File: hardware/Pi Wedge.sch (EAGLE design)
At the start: 9 parts

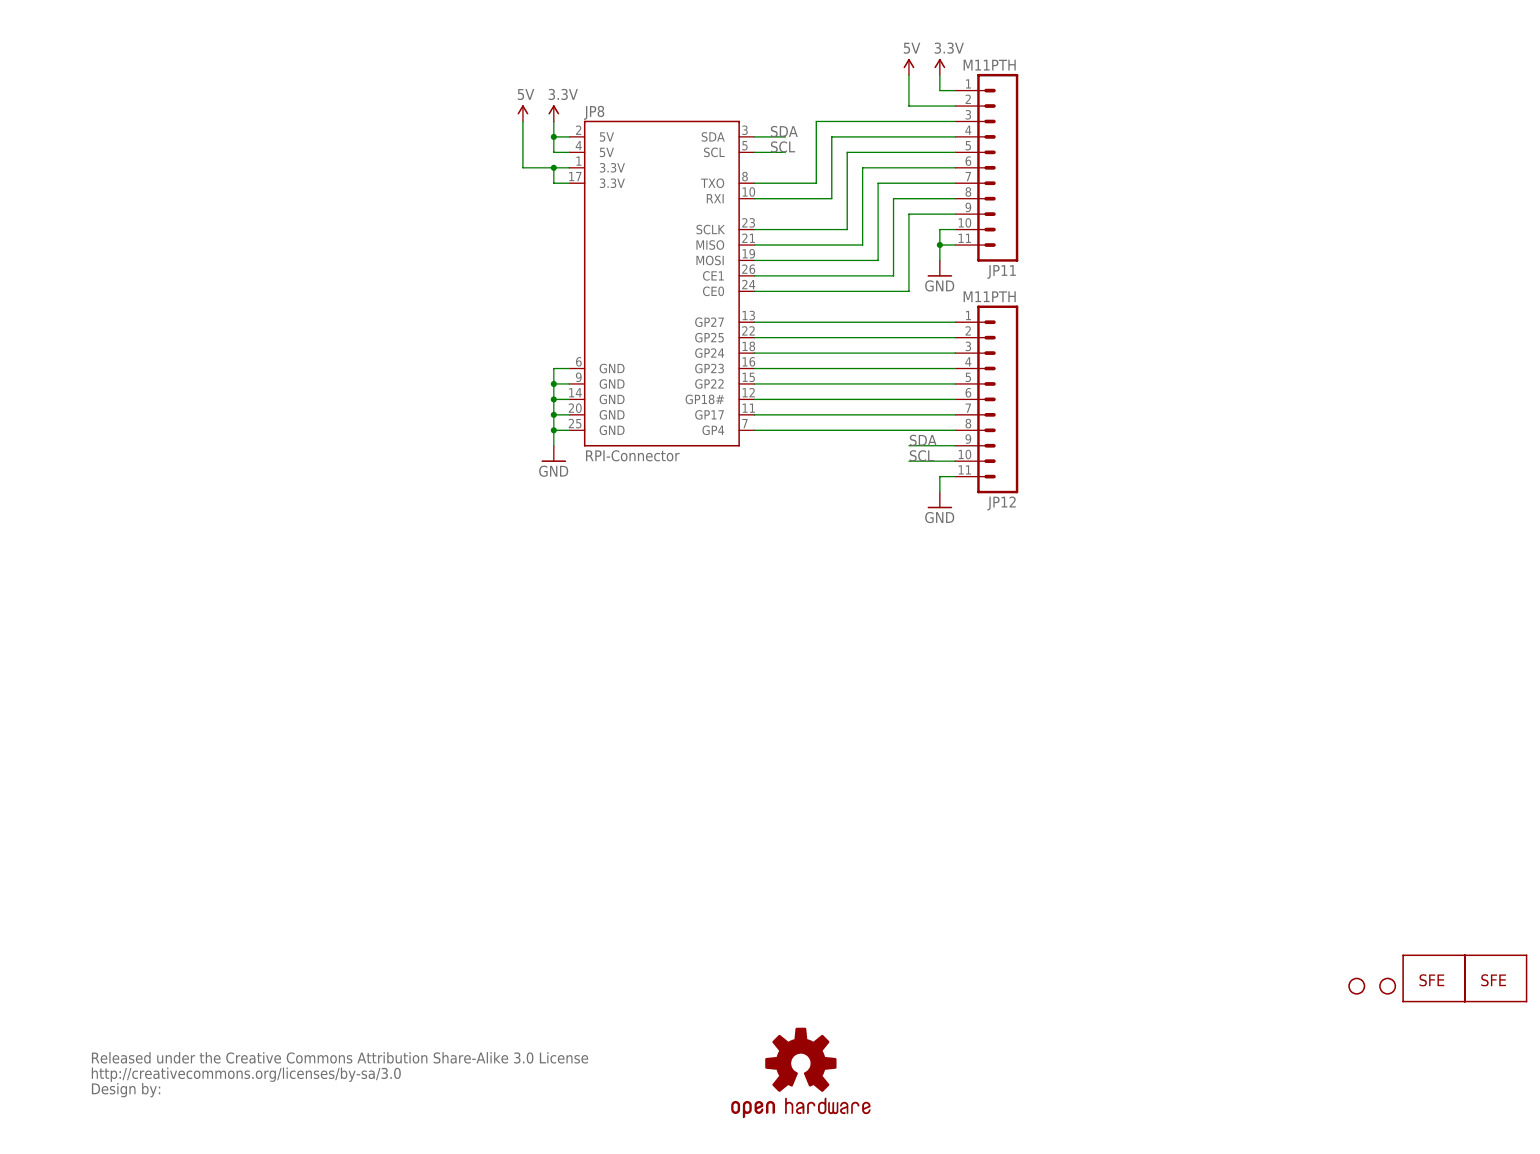
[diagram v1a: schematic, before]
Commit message: Adjusting everything.
Reoriented connectors, added 6-pin FTDI header and extra access to power
and ground.
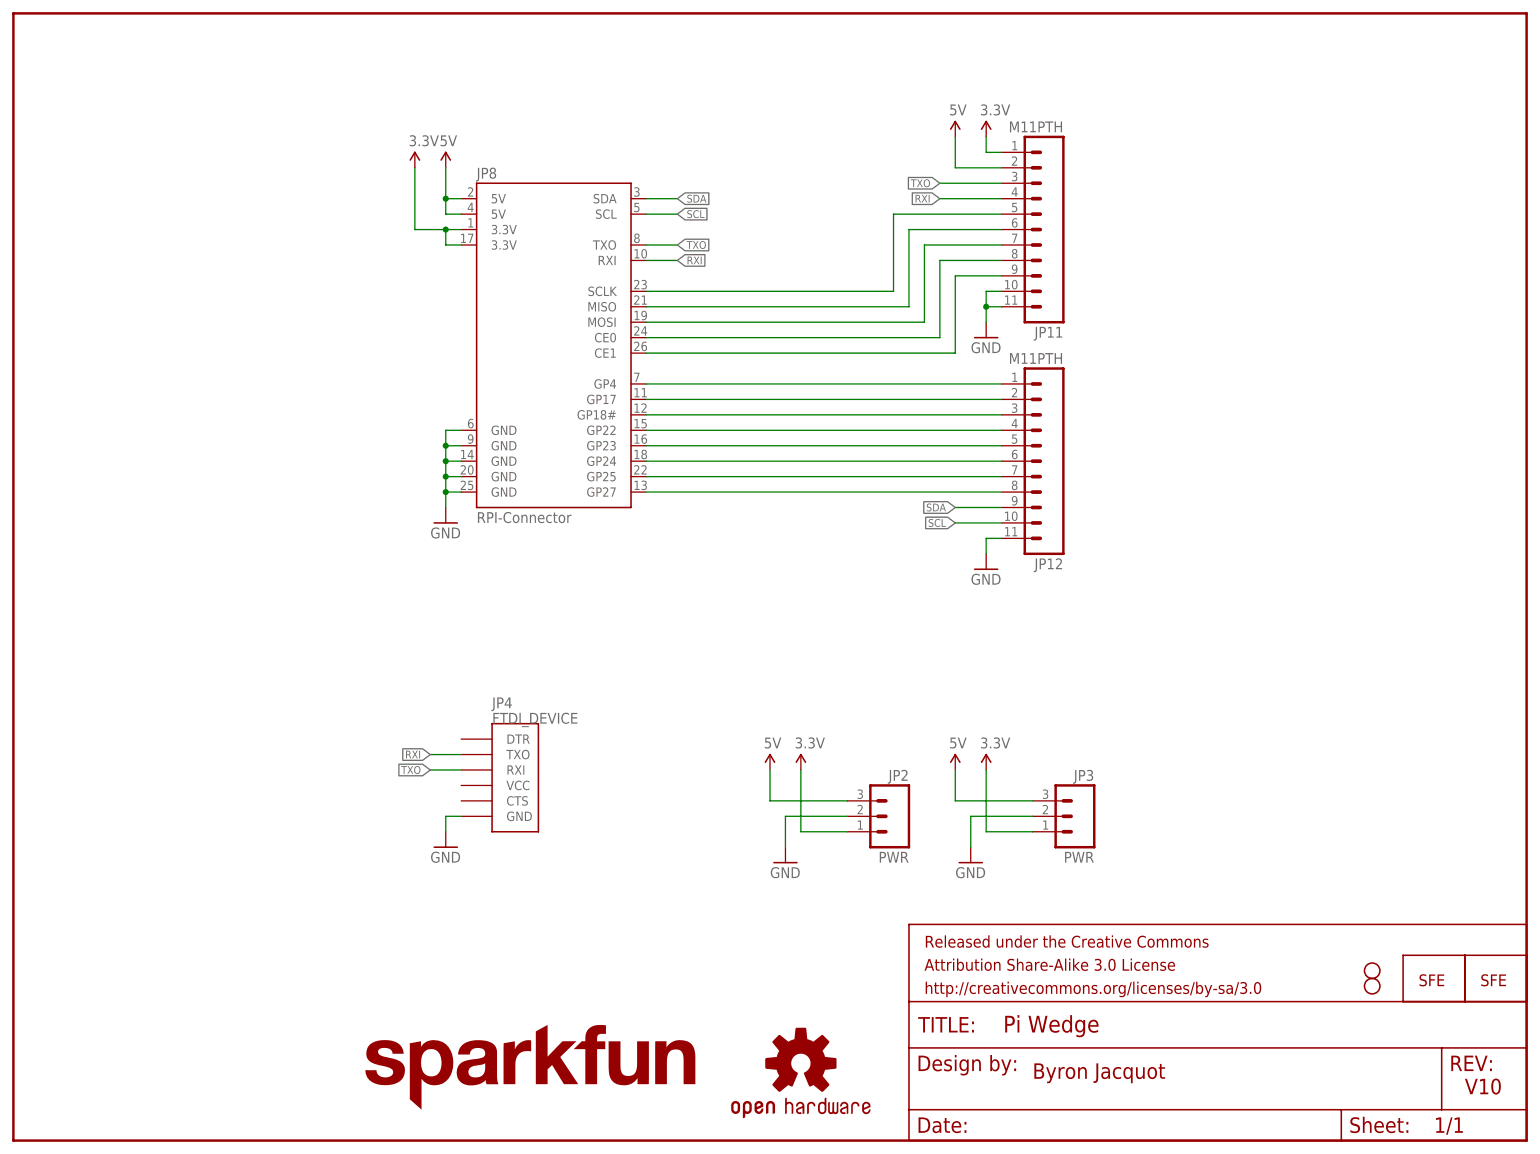
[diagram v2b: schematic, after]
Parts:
- removed U$2: CREATIVE_COMMONS, SparkFun:CREATIVE_COMMONS
- added FRAME2: FRAME-LETTER, SparkFun-Aesthetics:FRAME-LETTER
- added JP4: FTDI_DEVICE, SparkFun-Connectors:FTDI_DEVICE
- added LOGO1: SFE_LOGO_NAME.2_INCH, SparkFun-Aesthetics:SFE_LOGO_NAME.2_INCH
- added STANDOFF1, STANDOFF2: STAND-OFF, SparkFun-Electromechanical:STAND-OFF
- JP2, JP3: value STAND-OFF -> PWR; device SparkFun:STAND-OFF -> SparkFun-Connectors:M03PTH
- JP8: device Testing:RASPBERRYPI-GPIOPTH -> SparkFun-Boards:RASPBERRYPI-GPIOPTH
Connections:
- removed net CE2: JP11.9, JP8.CE0
- removed net GP17: JP12.7, JP8.GP17
- removed net GP18: JP12.6, JP8.GP18#
- removed net GP22: JP12.5, JP8.GP22
- removed net GP23: JP12.4, JP8.GP23
- removed net GP24: JP12.3, JP8.GP24
- removed net GP25: JP12.2, JP8.GP25
- removed net GP27: JP12.1, JP8.GP27
- removed net GP4: JP12.8, JP8.GP4
- new net CE0: JP11.8, JP8.CE0
- new net GPIO17: JP12.2, JP8.GP17
- new net GPIO18: JP12.3, JP8.GP18#
- new net GPIO22: JP12.4, JP8.GP22
- new net GPIO23: JP12.5, JP8.GP23
- new net GPIO24: JP12.6, JP8.GP24
- new net GPIO25: JP12.7, JP8.GP25
- new net GPIO27: JP12.8, JP8.GP27
- new net GPIO4: JP12.1, JP8.GP4
- net 3.3V: now also JP2.1, JP3.1, JP8.3.3V@1, JP8.3.3V@17; no longer JP8.5V@2, JP8.5V@4
- net 5V: now also JP2.3, JP3.3, JP8.5V@2, JP8.5V@4; no longer JP8.3.3V@1, JP8.3.3V@17
- net CE1: now also JP11.9; no longer JP11.8
- net GND: now also JP2.2, JP3.2, JP4.GND
- net RXI: now also JP4.TXO
- net TXO: now also JP4.RXI
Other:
- note added: "Byron Jacquot"
- note added: "V10"
- moved on the sheet: JP11, JP12, JP8

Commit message: Updates based on group review
Including:
-Kit footprints for the DIP-spaced headers
-Wider overall spacing, so power pads match a breadboard more closely
-PTH decoupling caps on power lines
-Rounded corners.
-Vector text
-Respecting keepout area around standoffs
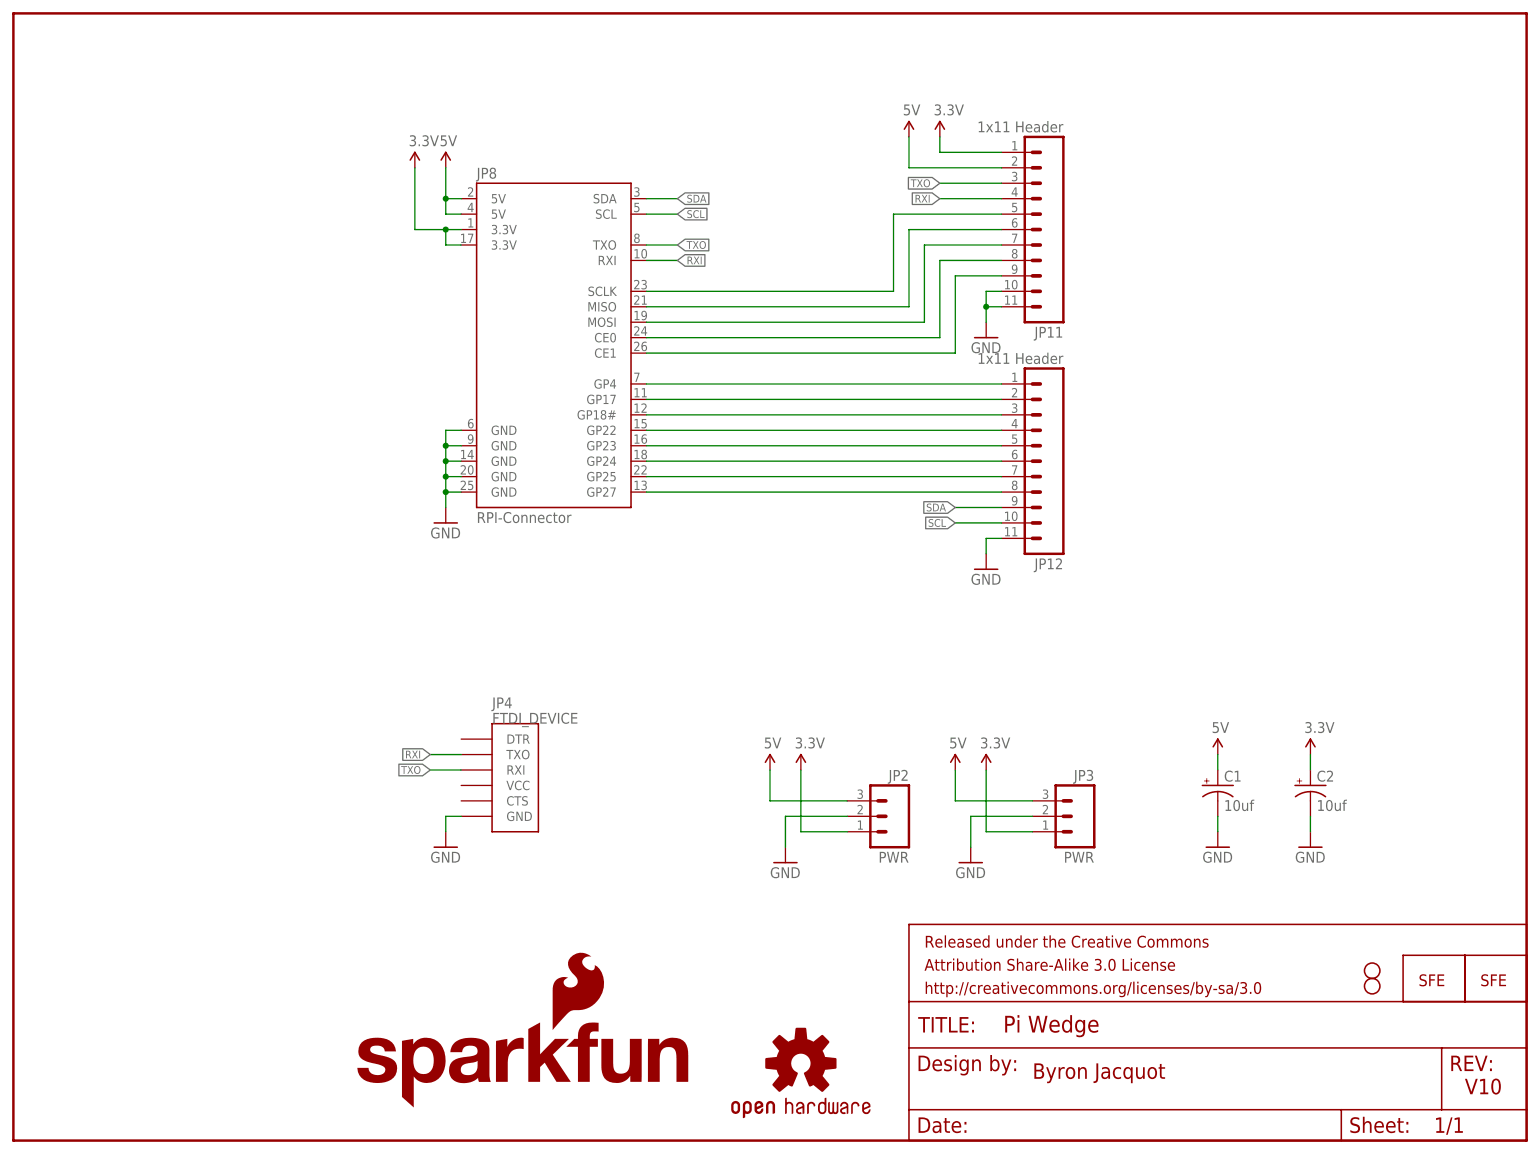
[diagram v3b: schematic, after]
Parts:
- added C1, C2: 10uf, SparkFun-Capacitors:10UF-25V-20%(PTH)KIT
- JP11, JP12: value M11PTH -> 1x11 Header; device SparkFun-Connectors:M11PTH -> SparkFun-Connectors:M111X11_NO_SILK_KIT
- LOGO1: value SFE_LOGO_NAME.2_INCH -> SFE_LOGO_NAME_FLAME.2_INCH; device SparkFun-Aesthetics:SFE_LOGO_NAME.2_INCH -> SparkFun-Aesthetics:SFE_LOGO_NAME_FLAME.2_INCH
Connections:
- net 3.3V: now also C2.+
- net 5V: now also C1.+
- net GND: now also C1.-, C2.-
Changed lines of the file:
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@@
 <part name="SUPPLY1" library="SparkFun-Aesthetics" deviceset="5V" device=""/>
 <part name="SUPPLY2" library="SparkFun-Aesthetics" deviceset="3.3V" device=""/>
-<part name="JP11" library="SparkFun-Connectors" deviceset="M11" device="PTH"/>
-<part name="JP12" library="SparkFun-Connectors" deviceset="M11" device="PTH"/>
+<part name="JP11" library="SparkFun-Connectors" deviceset="M11" device="1X11_NO_SILK_KIT" value="1x11 Header"/>
+<part name="JP12" library="SparkFun-Connectors" deviceset="M11" device="1X11_NO_SILK_KIT" value="1x11 Header"/>
 <part name="SUPPLY3" library="SparkFun-Aesthetics" deviceset="3.3V" device=""/>
 <part name="SUPPLY4" library="SparkFun-Aesthetics" deviceset="5V" device=""/>
@@
 <part name="SUPPLY7" library="SparkFun-Aesthetics" deviceset="3.3V" device=""/>
 <part name="SUPPLY8" library="SparkFun-Aesthetics" deviceset="3.3V" device=""/>
-<part name="LOGO1" library="SparkFun-Aesthetics" deviceset="SFE_LOGO_NAME" device=".2_INCH"/>
+<part name="LOGO1" library="SparkFun-Aesthetics" deviceset="SFE_LOGO_NAME_FLAME" device=".2_INCH"/>
 <part name="STANDOFF1" library="SparkFun-Electromechanical" deviceset="STAND-OFF" device=""/>
 <part name="STANDOFF2" library="SparkFun-Electromechanical" deviceset="STAND-OFF" device=""/>
 <part name="JP5" library="SparkFun" deviceset="LOGO-SFE" device="SK"/>
+<part name="C1" library="SparkFun-Capacitors" deviceset="10UF-25V-20%(PTH)" device="KIT" value="10uf"/>
+<part name="C2" library="SparkFun-Capacitors" deviceset="10UF-25V-20%(PTH)" device="KIT" value="10uf"/>
+<part name="GND4" library="SparkFun" deviceset="GND" device=""/>
+<part name="GND8" library="SparkFun" deviceset="GND" device=""/>
+<part name="SUPPLY9" library="SparkFun-Aesthetics" deviceset="5V" device=""/>
+<part name="SUPPLY10" library="SparkFun-Aesthetics" deviceset="3.3V" device=""/>
 </parts>
 <sheets>
@@
 <instance part="JP11" gate="G$1" x="172.72" y="149.86" rot="R180"/>
 <instance part="JP12" gate="G$1" x="172.72" y="111.76" rot="R180"/>
-<instance part="SUPPLY3" gate="G$1" x="160.02" y="165.1"/>
-<instance part="SUPPLY4" gate="G$1" x="154.94" y="165.1"/>
+<instance part="SUPPLY3" gate="G$1" x="152.4" y="165.1"/>
+<instance part="SUPPLY4" gate="G$1" x="147.32" y="165.1"/>
 <instance part="GND6" gate="1" x="160.02" y="132.08"/>
 <instance part="GND7" gate="1" x="160.02" y="93.98"/>
@@
 <instance part="STANDOFF2" gate="G$1" x="223.52" y="27.94"/>
 <instance part="JP5" gate="G$1" x="231.14" y="25.4"/>
+<instance part="C1" gate="G$1" x="198.12" y="58.42"/>
+<instance part="C2" gate="G$1" x="213.36" y="58.42"/>
+<instance part="GND4" gate="1" x="198.12" y="48.26"/>
+<instance part="GND8" gate="1" x="213.36" y="48.26"/>
+<instance part="SUPPLY9" gate="G$1" x="198.12" y="63.5"/>
+<instance part="SUPPLY10" gate="G$1" x="213.36" y="63.5"/>
 </instances>
 <busses>
@@
 <wire x1="127" y1="53.34" x2="137.16" y2="53.34" width="0.1524" layer="91"/>
 </segment>
+<segment>
+<pinref part="C2" gate="G$1" pin="-"/>
+<pinref part="GND8" gate="1" pin="GND"/>
+<wire x1="213.36" y1="53.34" x2="213.36" y2="50.8" width="0.2032" layer="91"/>
+</segment>
+<segment>
+<pinref part="C1" gate="G$1" pin="-"/>
+<pinref part="GND4" gate="1" pin="GND"/>
+<wire x1="198.12" y1="53.34" x2="198.12" y2="50.8" width="0.2032" layer="91"/>
+</segment>
 </net>
 <net name="5V" class="0">
 <segment>
 <pinref part="JP11" gate="G$1" pin="2"/>
-<wire x1="162.56" y1="160.02" x2="154.94" y2="160.02" width="0.1524" layer="91"/>
-<wire x1="154.94" y1="160.02" x2="154.94" y2="165.1" width="0.1524" layer="91"/>
+<wire x1="162.56" y1="160.02" x2="147.32" y2="160.02" width="0.1524" layer="91"/>
+<wire x1="147.32" y1="160.02" x2="147.32" y2="165.1" width="0.1524" layer="91"/>
 <pinref part="SUPPLY4" gate="G$1" pin="5V"/>
 </segment>
@@
 <wire x1="124.46" y1="55.88" x2="137.16" y2="55.88" width="0.1524" layer="91"/>
 </segment>
+<segment>
+<pinref part="SUPPLY9" gate="G$1" pin="5V"/>
+<pinref part="C1" gate="G$1" pin="+"/>
+<wire x1="198.12" y1="63.5" x2="198.12" y2="60.96" width="0.2032" layer="91"/>
+</segment>
 </net>
 <net name="3.3V" class="0">
 <segment>
 <pinref part="JP11" gate="G$1" pin="1"/>
-<wire x1="162.56" y1="162.56" x2="160.02" y2="162.56" width="0.1524" layer="91"/>
-<wire x1="160.02" y1="162.56" x2="160.02" y2="165.1" width="0.1524" layer="91"/>
+<wire x1="162.56" y1="162.56" x2="152.4" y2="162.56" width="0.1524" layer="91"/>
+<wire x1="152.4" y1="162.56" x2="152.4" y2="165.1" width="0.1524" layer="91"/>
 <pinref part="SUPPLY3" gate="G$1" pin="3.3V"/>
 </segment>
@@
 <wire x1="129.54" y1="50.8" x2="137.16" y2="50.8" width="0.1524" layer="91"/>
 </segment>
-</net>
+<segment>
+<pinref part="SUPPLY10" gate="G$1" pin="3.3V"/>
+<pinref part="C2" gate="G$1" pin="+"/>
+<wire x1="213.36" y1="63.5" x2="213.36" y2="60.96" width="0.2032" layer="91"/>
+</segment>
+</net>

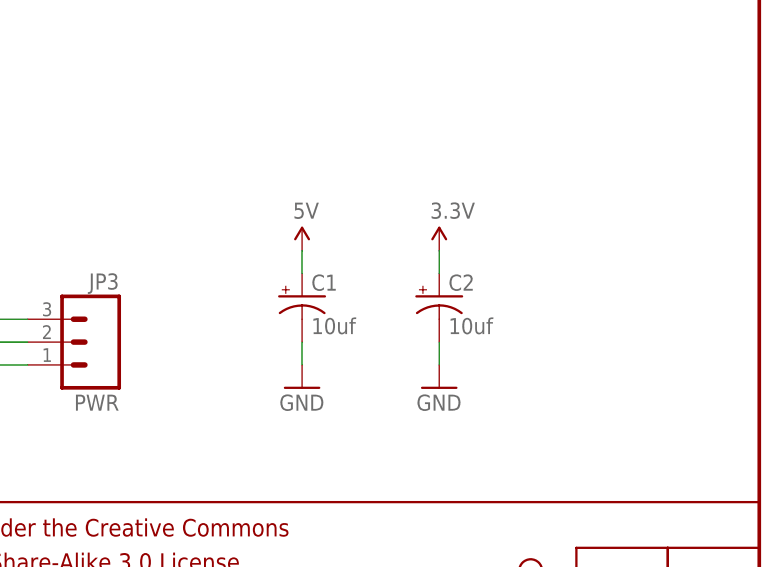
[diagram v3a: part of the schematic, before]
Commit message: Touchup to Cap names
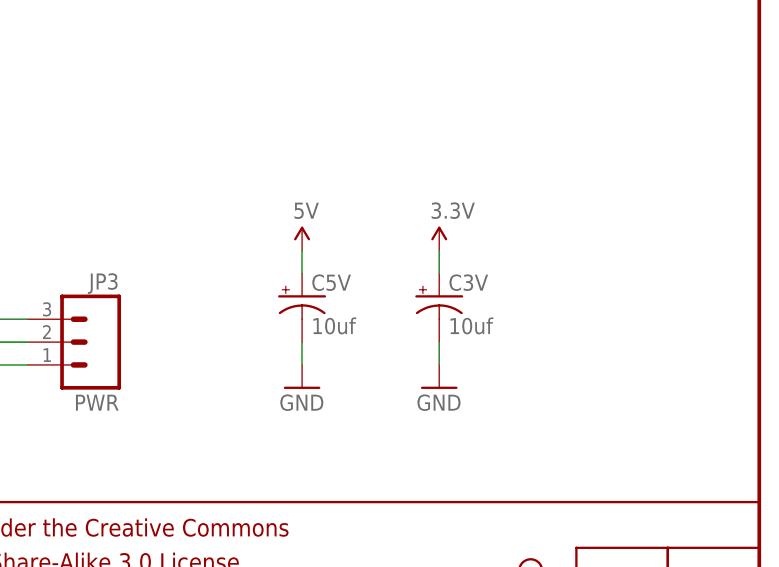
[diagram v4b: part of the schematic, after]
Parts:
- renumbered C1 to C5V, C2 to C3V
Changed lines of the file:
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@@
 <part name="STANDOFF2" library="SparkFun-Electromechanical" deviceset="STAND-OFF" device=""/>
 <part name="JP5" library="SparkFun" deviceset="LOGO-SFE" device="SK"/>
-<part name="C1" library="SparkFun-Capacitors" deviceset="10UF-25V-20%(PTH)" device="KIT" value="10uf"/>
-<part name="C2" library="SparkFun-Capacitors" deviceset="10UF-25V-20%(PTH)" device="KIT" value="10uf"/>
+<part name="C5V" library="SparkFun-Capacitors" deviceset="10UF-25V-20%(PTH)" device="KIT" value="10uf"/>
+<part name="C3V" library="SparkFun-Capacitors" deviceset="10UF-25V-20%(PTH)" device="KIT" value="10uf"/>
 <part name="GND4" library="SparkFun" deviceset="GND" device=""/>
 <part name="GND8" library="SparkFun" deviceset="GND" device=""/>
@@
 <instance part="STANDOFF2" gate="G$1" x="223.52" y="27.94"/>
 <instance part="JP5" gate="G$1" x="231.14" y="25.4"/>
-<instance part="C1" gate="G$1" x="198.12" y="58.42"/>
-<instance part="C2" gate="G$1" x="213.36" y="58.42"/>
+<instance part="C5V" gate="G$1" x="198.12" y="58.42"/>
+<instance part="C3V" gate="G$1" x="213.36" y="58.42"/>
 <instance part="GND4" gate="1" x="198.12" y="48.26"/>
 <instance part="GND8" gate="1" x="213.36" y="48.26"/>
@@
 </segment>
 <segment>
-<pinref part="C2" gate="G$1" pin="-"/>
+<pinref part="C3V" gate="G$1" pin="-"/>
 <pinref part="GND8" gate="1" pin="GND"/>
 <wire x1="213.36" y1="53.34" x2="213.36" y2="50.8" width="0.2032" layer="91"/>
 </segment>
 <segment>
-<pinref part="C1" gate="G$1" pin="-"/>
+<pinref part="C5V" gate="G$1" pin="-"/>
 <pinref part="GND4" gate="1" pin="GND"/>
 <wire x1="198.12" y1="53.34" x2="198.12" y2="50.8" width="0.2032" layer="91"/>
@@
 <segment>
 <pinref part="SUPPLY9" gate="G$1" pin="5V"/>
-<pinref part="C1" gate="G$1" pin="+"/>
+<pinref part="C5V" gate="G$1" pin="+"/>
 <wire x1="198.12" y1="63.5" x2="198.12" y2="60.96" width="0.2032" layer="91"/>
 </segment>
@@
 <segment>
 <pinref part="SUPPLY10" gate="G$1" pin="3.3V"/>
-<pinref part="C2" gate="G$1" pin="+"/>
+<pinref part="C3V" gate="G$1" pin="+"/>
 <wire x1="213.36" y1="63.5" x2="213.36" y2="60.96" width="0.2032" layer="91"/>
 </segment>
